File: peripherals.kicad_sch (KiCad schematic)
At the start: 75 parts, among them J1 USB-C_USB4105-GF-A, J10 PinHeader_1x6_P2.54mm_SMD_Hor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, J4 Conn_FFC_WE_68715014522_ONE-S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, J5 PinHeader_2x5_P1.27mm_SMD, J6 Conn_FFC_WE_68715014522_ONE-S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, J8 SM04B-SRSS-TB-LF-SN, J9 SM06B-GHS-TB-LF-SN, SW1 SW_CVS-02B, U11 LIFCL-40-9BG256C, U13 DIO7553ST6, U14 DIO7553ST6, U19 DIO7553ST6, U20 FT230X_QFN

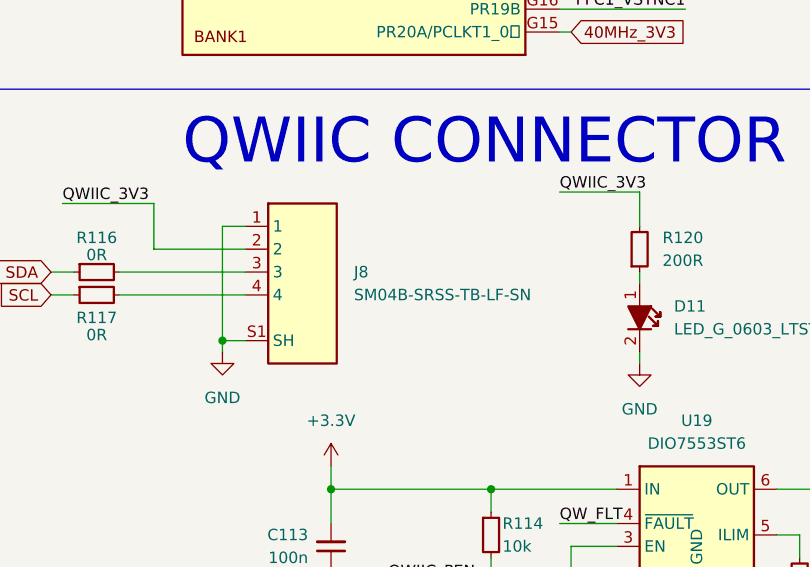
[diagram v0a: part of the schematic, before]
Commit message: [#55653] Update SM04B-SRSS-TB(LF)(SN)
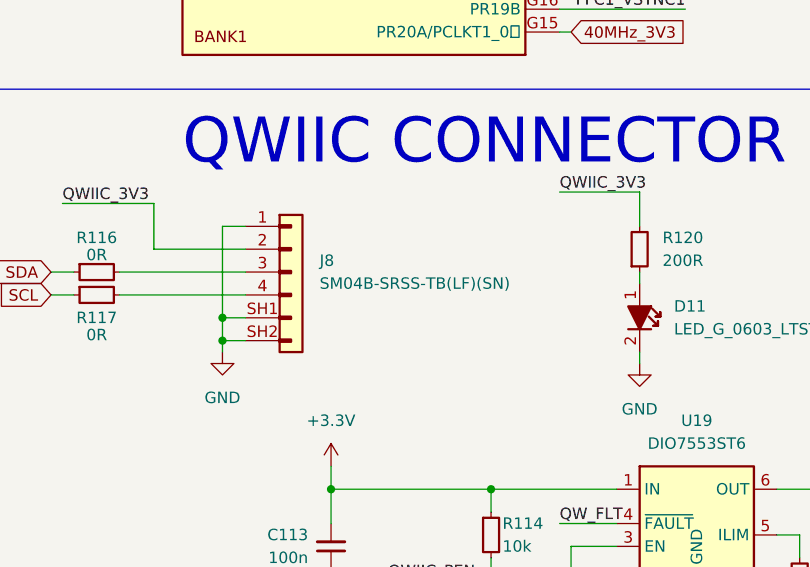
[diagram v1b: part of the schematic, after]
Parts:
- J8: footprint sdi-mipi-video-converter-footprints:SM04B-SRSS-TB-LF-SN -> antmicro-footprints:Conn_JST_SH_1x4_SM04B-SRSS-TB-LF-SN; symbol sdi-mipi-video-converter:SM04B-SRSS-TB-LF-SN -> antmicroWire2BoardConnectors:JST_SH_1x4_SM04B-SRSS-TB-LF-SN; Manufacturer JST -> JST Automotive Connectors
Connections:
- net GND: now also J8.SH1, J8.SH2; no longer J8.S1 (SH), J8.S2 (SH)
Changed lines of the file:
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@@
   (junction (at 96.52 276.86) (diameter 0) (color 0 0 0 0)
   )
+  (junction (at 41.275 210.82) (diameter 0) (color 0 0 0 0)
+  )
   (junction (at 368.3 204.47) (diameter 0) (color 0 0 0 0)
   )
@@
     (stroke (width 0) (type default))
   )
-  (wire (pts (xy 41.275 200.66) (xy 41.275 213.36))
+  (wire (pts (xy 41.275 200.66) (xy 41.275 210.82))
     (stroke (width 0) (type default))
   )
@@
     (stroke (width 0) (type default))
   )
+  (wire (pts (xy 41.275 210.82) (xy 43.815 210.82))
+    (stroke (width 0) (type default))
+  )
   (wire (pts (xy 78.74 138.43) (xy 92.71 138.43))
     (stroke (width 0) (type default))
@@
     (stroke (width 0) (type default))
   )
+  (wire (pts (xy 41.275 210.82) (xy 41.275 213.36))
+    (stroke (width 0) (type default))
+  )
   (wire (pts (xy 102.87 234.95) (xy 105.41 234.95))
     (stroke (width 0) (type default))
@@
     )
   )
-  (symbol (lib_id "sdi-mipi-video-converter:SM04B-SRSS-TB-LF-SN") (at 43.815 200.66 0) (unit 1)
-    (in_bom yes) (on_board yes) (dnp no) (fields_autoplaced)
-    (property "Reference" "J8" (at 55.88 205.7399 0)
+  (symbol (lib_id "antmicroWire2BoardConnectors:JST_SH_1x4_SM04B-SRSS-TB-LF-SN") (at 43.815 200.66 0) (unit 1)
+    (in_bom yes) (on_board yes) (dnp no)
+    (property "Reference" "J8" (at 52.07 204.47 0)
       (effects (font (size 1.27 1.27) (thickness 0.15)) (justify left))
     )
-    (property "Value" "SM04B-SRSS-TB-LF-SN" (at 55.88 208.2799 0)
-      (effects (font (size 1.27 1.27) (thickness 0.15)) (justify left))
+    (property "Value" "SM04B-SRSS-TB-LF-SN" (at 52.07 207.01 0)
+      (effects (font (size 1.27 1.27) (thickness 0.15)) (justify left) hide)
     )
-    (property "Footprint" "sdi-mipi-video-converter-footprints:SM04B-SRSS-TB-LF-SN" (at 70.485 209.55 0)
+    (property "Footprint" "antmicro-footprints:Conn_JST_SH_1x4_SM04B-SRSS-TB-LF-SN" (at 70.485 210.82 0)
       (effects (font (size 1.27 1.27) (thickness 0.15)) (justify left bottom) hide)
     )
-    (property "Datasheet" "https://www.jst-mfg.com/product/pdf/eng/eSH.pdf" (at 70.485 212.09 0)
+    (property "Datasheet" "https://www.jst-mfg.com/product/pdf/eng/eSH.pdf" (at 70.485 213.36 0)
       (effects (font (size 1.27 1.27) (thickness 0.15)) (justify left bottom) hide)
     )
-    (property "MPN" "SM04B-SRSS-TB(LF)(SN)" (at 70.485 214.63 0)
-      (effects (font (size 1.27 1.27) (thickness 0.15)) (justify left bottom) hide)
+    (property "MPN" "SM04B-SRSS-TB(LF)(SN)" (at 52.07 207.01 0)
+      (effects (font (size 1.27 1.27) (thickness 0.15)) (justify left))
     )
-    (property "Manufacturer" "JST" (at 70.485 217.17 0)
+    (property "Manufacturer" "JST Automotive Connectors" (at 70.485 215.9 0)
       (effects (font (size 1.27 1.27) (thickness 0.15)) (justify left bottom) hide)
     )
-    (property "Author" "Antmicro" (at 70.485 219.71 0)
+    (property "Author" "Antmicro" (at 70.485 218.44 0)
       (effects (font (size 1.27 1.27) (thickness 0.15)) (justify left bottom) hide)
     )
-    (property "License" "Apache-2.0" (at 70.485 222.25 0)
+    (property "License" "Apache-2.0" (at 70.485 220.98 0)
       (effects (font (size 1.27 1.27) (thickness 0.15)) (justify left bottom) hide)
     )
@@
     (pin "3")
     (pin "4")
-    (pin "S1")
-    (pin "S2")
+    (pin "SH1")
+    (pin "SH2")
     (instances
       (project "sdi-mipi-video-converter"

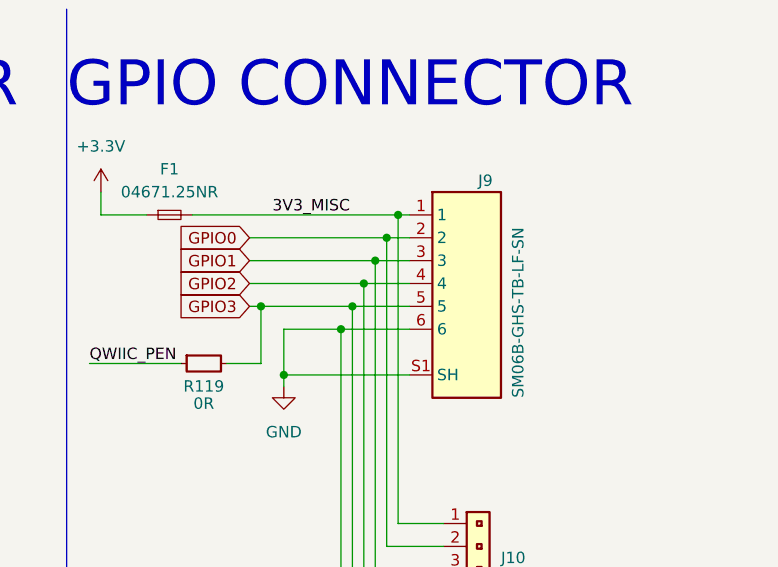
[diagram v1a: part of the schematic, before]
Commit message: [#55653] Update SM06B-GHS-TB(LF)(SN)
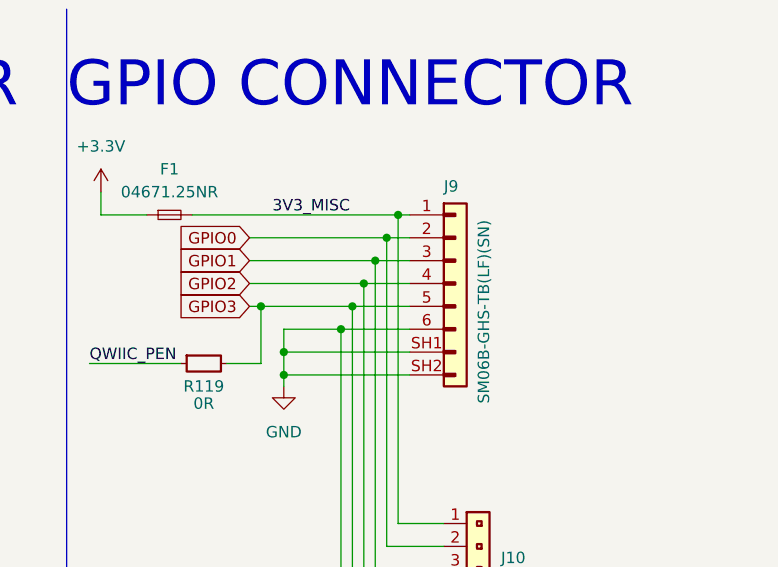
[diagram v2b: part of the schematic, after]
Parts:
- J9: footprint sdi-mipi-video-converter-footprints:JST_SM06B-SRSS-TB-LF-SN -> antmicro-footprints:Conn_JST_GH_1x6_SM06B-GHS-TB-LF-SN; symbol sdi-mipi-video-converter:SM06B-GHS-TB-LF-SN -> antmicroWire2BoardConnectors:JST_GH_1x6_SM06B-GHS-TB-LF-SN; Manufacturer JST -> JST Automotive Connectors
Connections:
- net GND: now also J9.SH1, J9.SH2; no longer J9.S1 (SH), J9.S2 (SH)
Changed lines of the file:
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@@
   (junction (at 374.65 38.1) (diameter 0) (color 0 0 0 0)
   )
+  (junction (at 363.22 50.8) (diameter 0) (color 0 0 0 0)
+  )
   (junction (at 53.34 229.87) (diameter 0) (color 0 0 0 0)
   )
@@
     (stroke (width 0) (type default))
   )
-  (wire (pts (xy 363.22 53.34) (xy 363.22 48.26))
+  (wire (pts (xy 363.22 53.34) (xy 363.22 50.8))
     (stroke (width 0) (type default))
   )
@@
     (stroke (width 0) (type default))
   )
+  (wire (pts (xy 363.22 50.8) (xy 377.19 50.8))
+    (stroke (width 0) (type default))
+  )
   (wire (pts (xy 255.27 57.15) (xy 252.73 57.15))
     (stroke (width 0) (type default))
@@
     (stroke (width 0) (type default))
   )
+  (wire (pts (xy 363.22 50.8) (xy 363.22 48.26))
+    (stroke (width 0) (type default))
+  )
   (wire (pts (xy 299.72 52.07) (xy 300.99 52.07))
     (stroke (width 0) (type default))
@@
     )
   )
-  (symbol (lib_id "sdi-mipi-video-converter:SM06B-GHS-TB-LF-SN") (at 377.19 35.56 0) (unit 1)
+  (symbol (lib_id "antmicroWire2BoardConnectors:JST_GH_1x6_SM06B-GHS-TB-LF-SN") (at 377.19 35.56 0) (unit 1)
     (in_bom yes) (on_board yes) (dnp no)
-    (property "Reference" "J9" (at 384.81 31.75 0)
+    (property "Reference" "J9" (at 381 32.385 0)
       (effects (font (size 1.27 1.27) (thickness 0.15)) (justify left))
     )
     (property "Value" "SM06B-GHS-TB-LF-SN" (at 389.255 55.88 90)
-      (effects (font (size 1.27 1.27) (thickness 0.15)) (justify left))
+      (effects (font (size 1.27 1.27) (thickness 0.15)) (justify left) hide)
     )
-    (property "Footprint" "sdi-mipi-video-converter-footprints:JST_SM06B-SRSS-TB-LF-SN" (at 405.13 45.72 0)
+    (property "Footprint" "antmicro-footprints:Conn_JST_GH_1x6_SM06B-GHS-TB-LF-SN" (at 403.86 45.72 0)
       (effects (font (size 1.27 1.27) (thickness 0.15)) (justify left bottom) hide)
     )
-    (property "Datasheet" "https://www.jst-mfg.com/product/pdf/eng/eGH.pdf" (at 405.13 48.26 0)
+    (property "Datasheet" "https://www.jst-mfg.com/product/pdf/eng/eGH.pdf" (at 403.86 48.26 0)
       (effects (font (size 1.27 1.27) (thickness 0.15)) (justify left bottom) hide)
     )
-    (property "MPN" "SM06B-GHS-TB(LF)(SN)" (at 405.13 50.8 0)
-      (effects (font (size 1.27 1.27) (thickness 0.15)) (justify left bottom) hide)
+    (property "MPN" "SM06B-GHS-TB(LF)(SN)" (at 385.445 56.515 90)
+      (effects (font (size 1.27 1.27) (thickness 0.15)) (justify left))
     )
-    (property "Manufacturer" "JST" (at 405.13 53.34 0)
+    (property "Manufacturer" "JST Automotive Connectors" (at 403.86 50.8 0)
       (effects (font (size 1.27 1.27) (thickness 0.15)) (justify left bottom) hide)
     )
-    (property "Author" "Antmicro" (at 405.13 55.88 0)
+    (property "Author" "Antmicro" (at 403.86 53.34 0)
       (effects (font (size 1.27 1.27) (thickness 0.15)) (justify left bottom) hide)
     )
-    (property "License" "Apache-2.0" (at 405.13 58.42 0)
+    (property "License" "Apache-2.0" (at 403.86 55.88 0)
       (effects (font (size 1.27 1.27) (thickness 0.15)) (justify left bottom) hide)
     )
@@
     (pin "5")
     (pin "6")
-    (pin "S1")
-    (pin "S2")
+    (pin "SH1")
+    (pin "SH2")
     (instances
       (project "sdi-mipi-video-converter"

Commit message: [#55653] Update TSM-106-01-T-SH
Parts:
- J10: footprint sdi-mipi-video-converter-footprints:PinHeader_1x6_TSM-106-01-T-SH -> antmicro-footprints:PinHeader_1x6_P2.54mm_SMD_Horizontal; symbol sdi-mipi-video-converter:PinHeader_1x6_P2.54mm_SMD_Horizontal -> antmicroGenericPinHeaders:PinHeader_1x6_P2.54mm_SMD_Horizontal
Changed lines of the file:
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@@
     )
   )
-  (symbol (lib_id "sdi-mipi-video-converter:PinHeader_1x6_P2.54mm_SMD_Horizontal") (at 381 69.85 0) (unit 1)
+  (symbol (lib_id "antmicroGenericPinHeaders:PinHeader_1x6_P2.54mm_SMD_Horizontal") (at 381 69.85 0) (unit 1)
     (in_bom yes) (on_board yes) (dnp no) (fields_autoplaced)
-    (property "Reference" "J10" (at 387.35 73.6599 0)
+    (property "Reference" "J10" (at 387.35 73.66 0)
       (effects (font (size 1.27 1.27) (thickness 0.15)) (justify left))
     )
@@
       (effects (font (size 1.27 1.27) (thickness 0.15)) (justify left bottom) hide)
     )
-    (property "Footprint" "sdi-mipi-video-converter-footprints:PinHeader_1x6_TSM-106-01-T-SH" (at 400.05 81.28 0)
+    (property "Footprint" "antmicro-footprints:PinHeader_1x6_P2.54mm_SMD_Horizontal" (at 400.05 81.28 0)
       (effects (font (size 1.27 1.27) (thickness 0.15)) (justify left bottom) hide)
     )
-    (property "Datasheet" "https://www.mouser.pl/datasheet/2/527/tsm-2854655.pdf" (at 400.05 83.82 0)
+    (property "Datasheet" "https://www.mouser.com/datasheet/2/527/tsm-2854655.pdf" (at 400.05 83.82 0)
       (effects (font (size 1.27 1.27) (thickness 0.15)) (justify left bottom) hide)
     )
@@
       (effects (font (size 1.27 1.27) (thickness 0.15)) (justify left bottom) hide)
     )
-    (property "MPN" "TSM-106-01-T-SH" (at 387.35 76.1999 0)
+    (property "MPN" "TSM-106-01-T-SH" (at 387.35 76.2 0)
       (effects (font (size 1.27 1.27) (thickness 0.15)) (justify left))
     )
@@
       (effects (font (size 1.27 1.27) (thickness 0.15)) (justify left bottom) hide)
     )
-    (property "DNP" "DNP" (at 387.35 78.7399 0)
+    (property "DNP" "DNP" (at 387.35 78.74 0)
       (effects (font (size 1.27 1.27)) (justify left))
     )

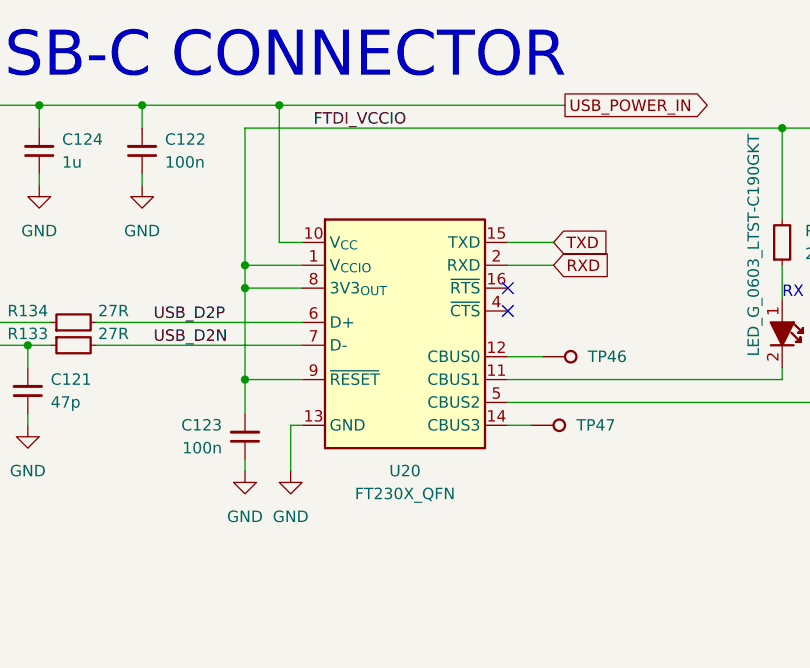
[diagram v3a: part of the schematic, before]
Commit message: [#55653] Update FT230X_QFN
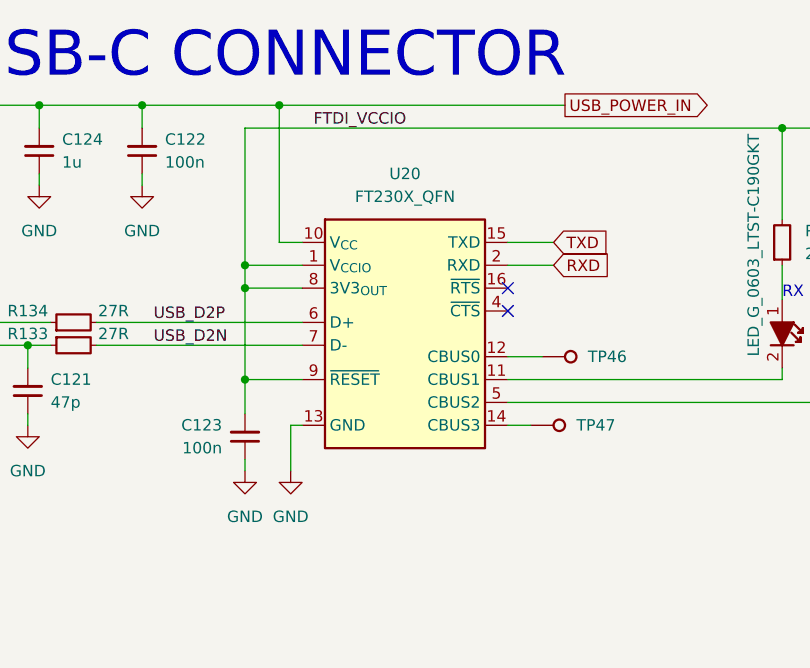
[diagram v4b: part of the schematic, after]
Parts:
- U20: footprint sdi-mipi-video-converter-footprints:QFN-16_1EP_4x4mm_P0.65mm -> antmicro-footprints:QFN-16-1EP_4x4mm_P0.65mm; symbol sdi-mipi-video-converter:FT230X_QFN -> antmicroInterfaceControllers:FT230X_QFN; Manufacturer FTDI -> FTDI Chip
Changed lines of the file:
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@@
     )
   )
-  (symbol (lib_id "sdi-mipi-video-converter:FT230X_QFN") (at 314.96 217.17 0) (unit 1)
+  (symbol (lib_id "antmicroInterfaceControllers:FT230X_QFN") (at 314.96 217.17 0) (unit 1)
     (in_bom yes) (on_board yes) (dnp no) (fields_autoplaced)
-    (property "Reference" "U20" (at 326.39 242.57 0)
+    (property "Reference" "U20" (at 326.39 209.55 0)
       (effects (font (size 1.27 1.27) (thickness 0.15)))
     )
-    (property "Value" "FT230X_QFN" (at 326.39 245.11 0)
+    (property "Value" "FT230X_QFN" (at 326.39 212.09 0)
       (effects (font (size 1.27 1.27) (thickness 0.15)))
     )
-    (property "Footprint" "sdi-mipi-video-converter-footprints:QFN-16_1EP_4x4mm_P0.65mm" (at 354.33 229.87 0)
+    (property "Footprint" "antmicro-footprints:QFN-16-1EP_4x4mm_P0.65mm" (at 354.33 229.87 0)
       (effects (font (size 1.27 1.27) (thickness 0.15)) (justify left bottom) hide)
     )
-    (property "Datasheet" "http://www.ftdichip.com/Support/Documents/DataSheets/ICs/DS_FT230X.pdf" (at 354.33 232.41 0)
+    (property "Datasheet" "https://ftdichip.com/wp-content/uploads/2021/10/DS_FT230X.pdf" (at 354.33 232.41 0)
       (effects (font (size 1.27 1.27) (thickness 0.15)) (justify left bottom) hide)
     )
-    (property "Manufacturer" "FTDI" (at 354.33 234.95 0)
+    (property "Manufacturer" "FTDI Chip" (at 354.33 234.95 0)
       (effects (font (size 1.27 1.27) (thickness 0.15)) (justify left bottom) hide)
     )

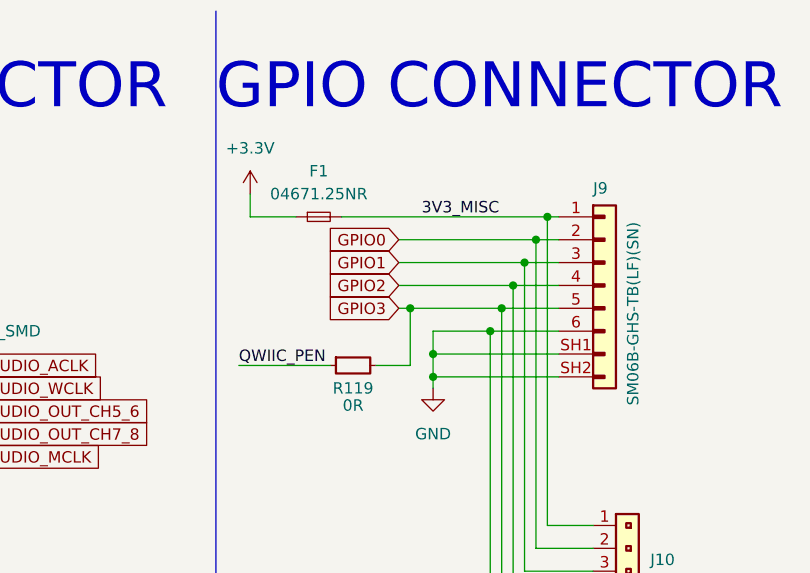
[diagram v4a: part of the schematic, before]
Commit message: [#55653] Update Conn_JST_GH_1x6_SM06B-SRSS-TB-LF-SN
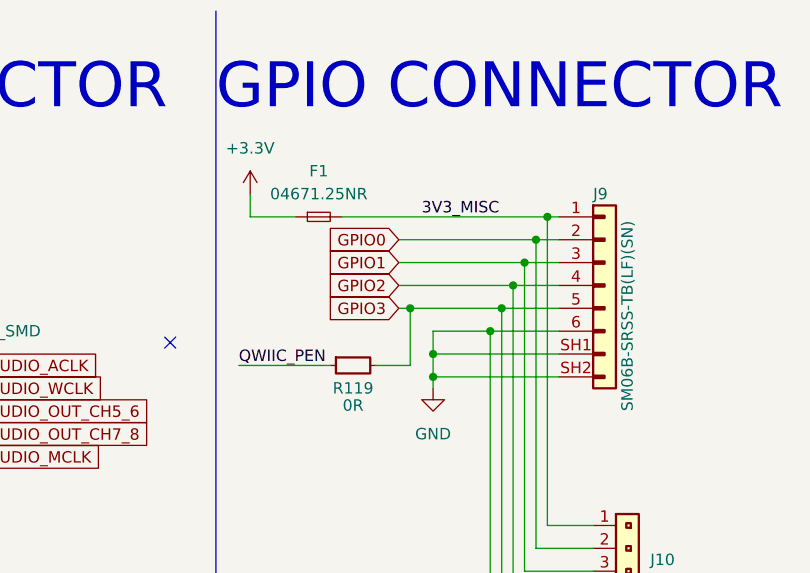
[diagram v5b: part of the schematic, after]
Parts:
- J9: footprint antmicro-footprints:Conn_JST_GH_1x6_SM06B-GHS-TB-LF-SN -> antmicro-footprints:Conn_JST_GH_1x6_SM06B-SRSS-TB-LF-SN; symbol antmicroWire2BoardConnectors:JST_GH_1x6_SM06B-GHS-TB-LF-SN -> antmicroWire2BoardConnectors:JST_GH_1x6_SM06B-SRSS-TB-LF-SN; MPN SM06B-GHS-TB(LF)(SN) -> SM06B-SRSS-TB(LF)(SN)
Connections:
- no-connect marks 41 -> 42
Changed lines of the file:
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@@
   (junction (at 71.12 240.03) (diameter 0) (color 0 0 0 0)
   )
+  (no_connect (at 334.01 49.53))
   (no_connect (at 194.31 128.27))
   (no_connect (at 194.31 130.81))
@@
     )
   )
-  (symbol (lib_id "antmicroWire2BoardConnectors:JST_GH_1x6_SM06B-GHS-TB-LF-SN") (at 377.19 35.56 0) (unit 1)
+  (symbol (lib_id "antmicroWire2BoardConnectors:JST_GH_1x6_SM06B-SRSS-TB-LF-SN") (at 377.19 35.56 0) (unit 1)
     (in_bom yes) (on_board yes) (dnp no)
-    (property "Reference" "J9" (at 381 32.385 0)
+    (property "Reference" "J9" (at 381 33.02 0)
       (effects (font (size 1.27 1.27) (thickness 0.15)) (justify left))
     )
@@
       (effects (font (size 1.27 1.27) (thickness 0.15)) (justify left) hide)
     )
-    (property "Footprint" "antmicro-footprints:Conn_JST_GH_1x6_SM06B-GHS-TB-LF-SN" (at 403.86 45.72 0)
+    (property "Footprint" "antmicro-footprints:Conn_JST_GH_1x6_SM06B-SRSS-TB-LF-SN" (at 403.86 45.72 0)
       (effects (font (size 1.27 1.27) (thickness 0.15)) (justify left bottom) hide)
     )
@@
       (effects (font (size 1.27 1.27) (thickness 0.15)) (justify left bottom) hide)
     )
-    (property "MPN" "SM06B-GHS-TB(LF)(SN)" (at 385.445 56.515 90)
+    (property "MPN" "SM06B-SRSS-TB(LF)(SN)" (at 384.81 57.15 90)
       (effects (font (size 1.27 1.27) (thickness 0.15)) (justify left))
     )

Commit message: [#55653] Loclib
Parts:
- J9: value SM06B-GHS-TB-LF-SN -> JST_GH_1x6_SM06B-SRSS-TB-LF-SN
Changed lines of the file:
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@@
   )
   (symbol (lib_id "antmicroWire2BoardConnectors:JST_GH_1x6_SM06B-SRSS-TB-LF-SN") (at 377.19 35.56 0) (unit 1)
-    (in_bom yes) (on_board yes) (dnp no)
-    (property "Reference" "J9" (at 381 33.02 0)
+    (in_bom yes) (on_board yes) (dnp no) (fields_autoplaced)
+    (property "Reference" "J9" (at 384.81 43.18 0)
       (effects (font (size 1.27 1.27) (thickness 0.15)) (justify left))
     )
-    (property "Value" "SM06B-GHS-TB-LF-SN" (at 389.255 55.88 90)
-      (effects (font (size 1.27 1.27) (thickness 0.15)) (justify left) hide)
+    (property "Value" "JST_GH_1x6_SM06B-SRSS-TB-LF-SN" (at 403.86 43.18 0)
+      (effects (font (size 1.27 1.27) (thickness 0.15)) (justify left bottom) hide)
     )
     (property "Footprint" "antmicro-footprints:Conn_JST_GH_1x6_SM06B-SRSS-TB-LF-SN" (at 403.86 45.72 0)
@@
       (effects (font (size 1.27 1.27) (thickness 0.15)) (justify left bottom) hide)
     )
-    (property "MPN" "SM06B-SRSS-TB(LF)(SN)" (at 384.81 57.15 90)
+    (property "MPN" "SM06B-SRSS-TB(LF)(SN)" (at 384.81 45.72 0)
       (effects (font (size 1.27 1.27) (thickness 0.15)) (justify left))
     )
